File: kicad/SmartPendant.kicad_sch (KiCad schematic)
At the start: 64 parts, among them J1 Conn_01x05, P1 FPC 0.5MM 40P Pull type H2.0m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, P2 KH-FG0.5-H2.0-6PIN, Q1 SS8050_C2150, U2 AMS1117-3.3, U3 MB85RC256VPNF

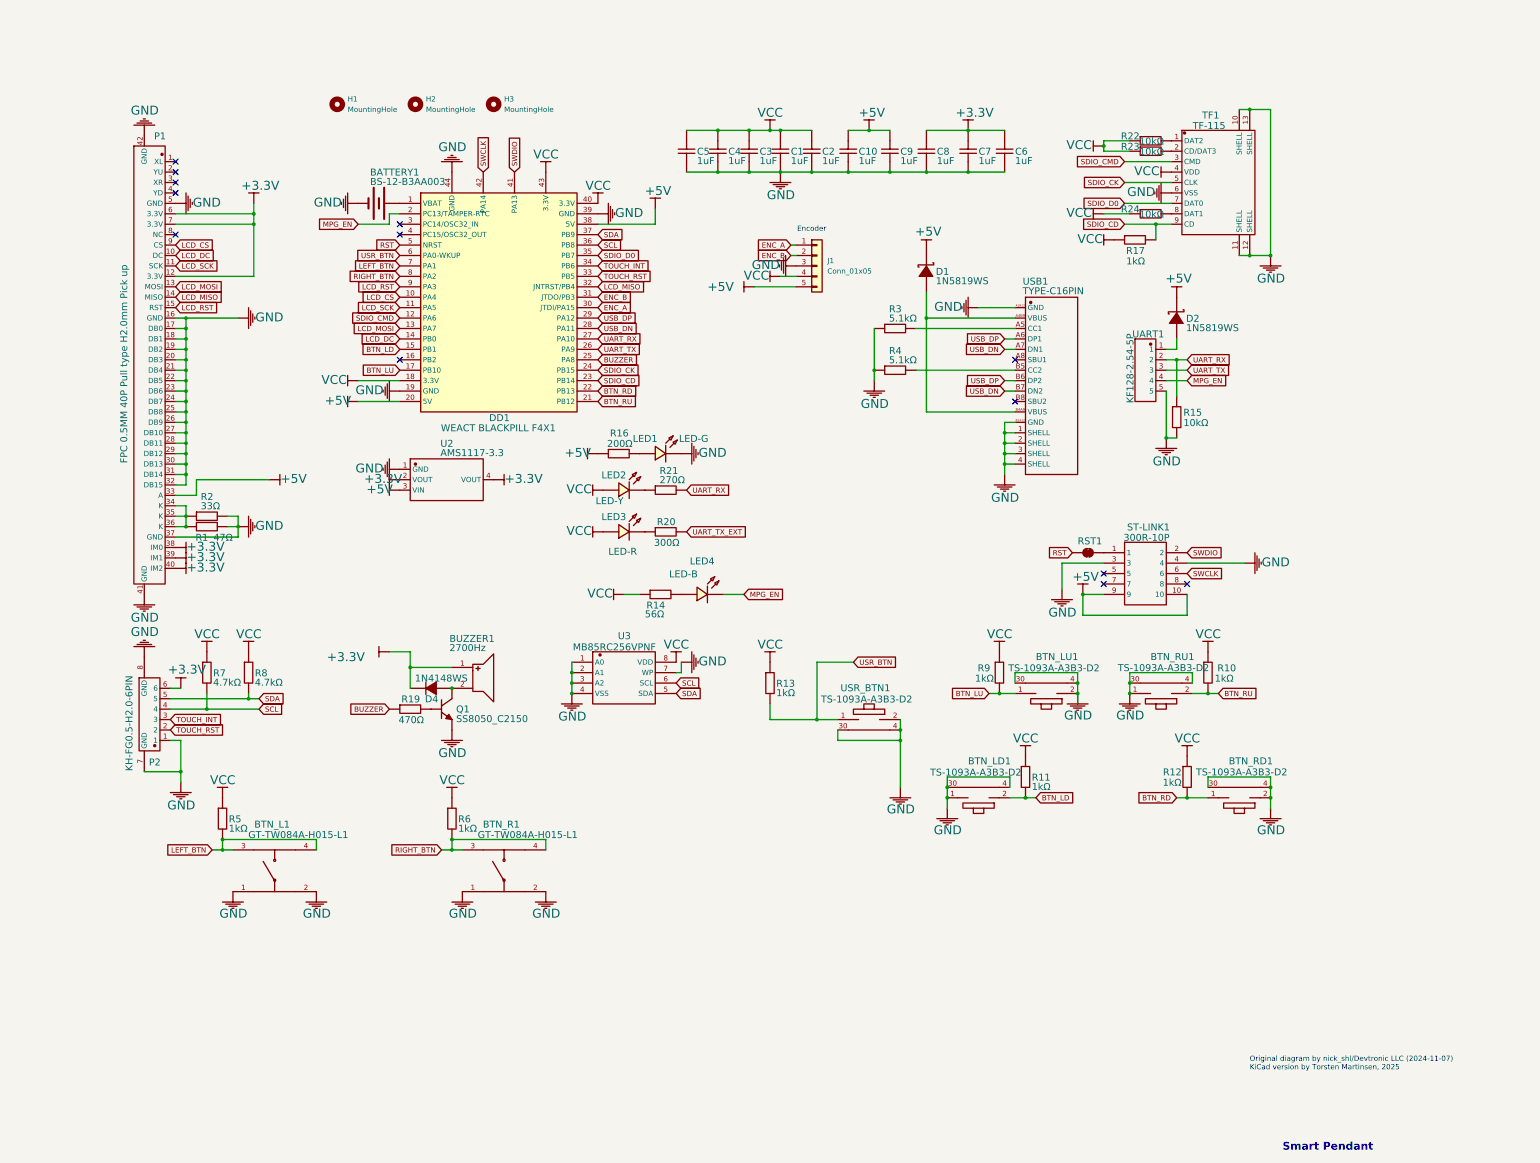
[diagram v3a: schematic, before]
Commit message: Add footprints.
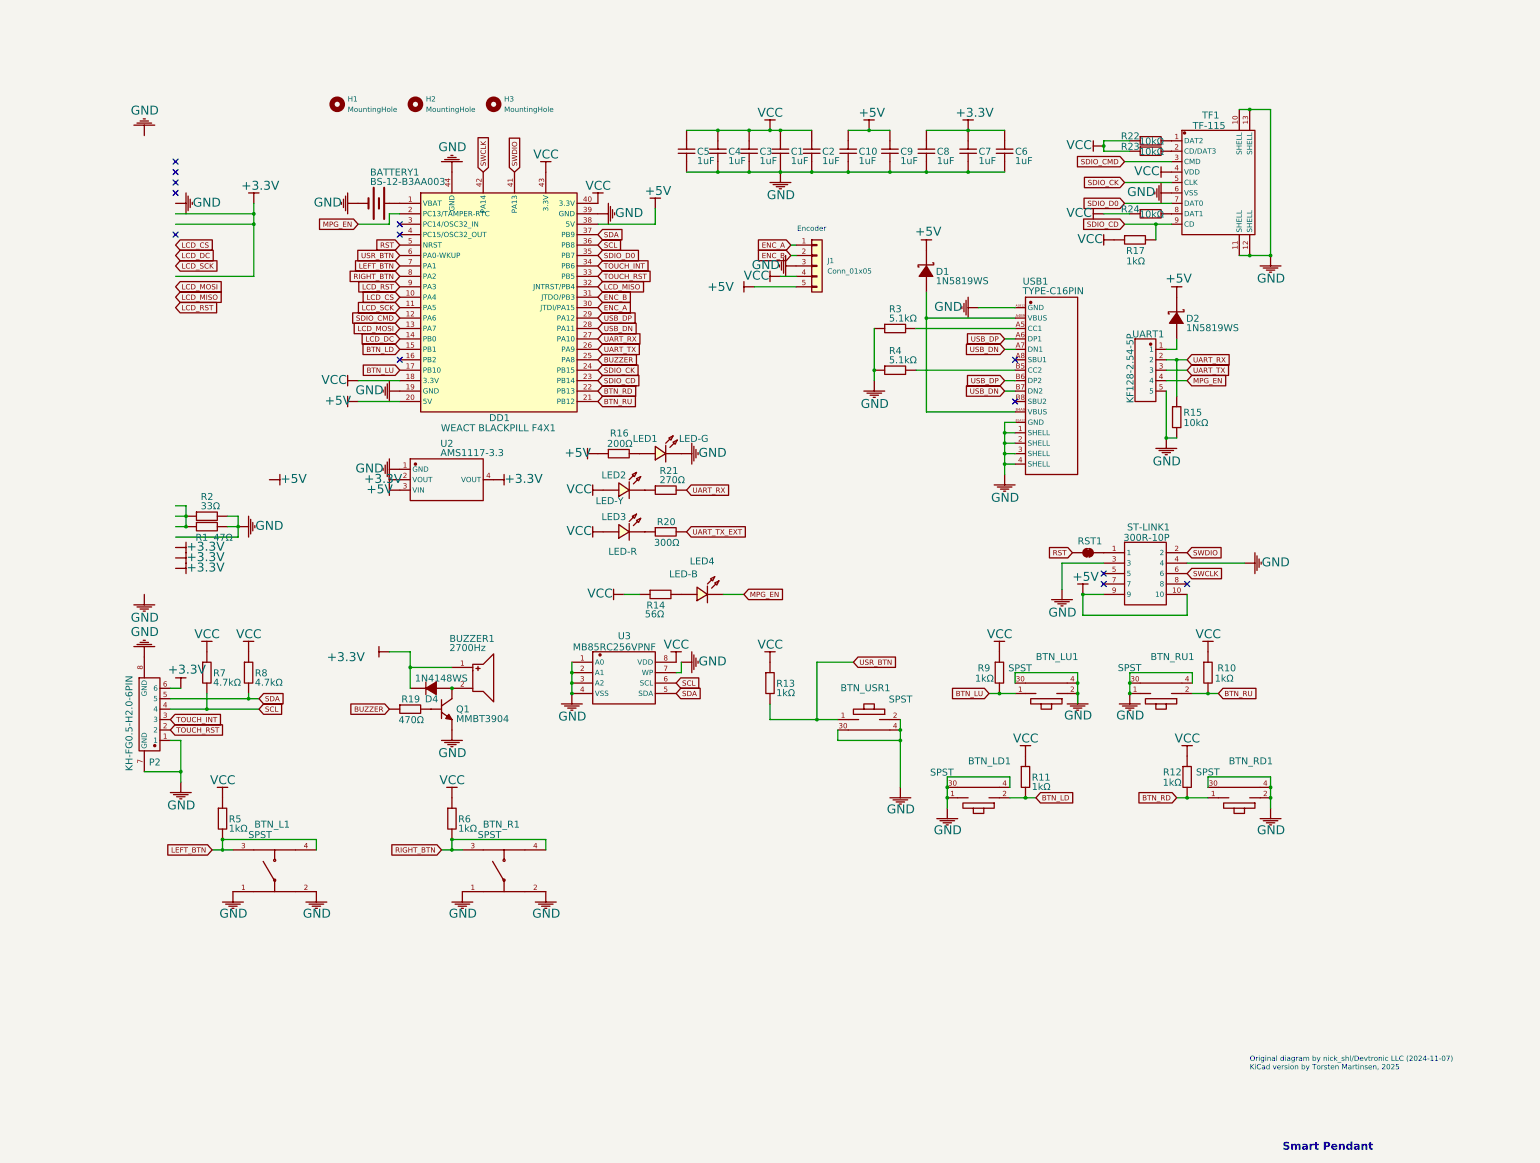
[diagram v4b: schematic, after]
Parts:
- removed P1: FPC 0.5MM 40P Pull type H2.0mm Pick up, symbol FPC 0.5MM 40P Pull type H2.0mm Pick up
- BATTERY1: footprint (none) -> Battery:BatteryHolder_Keystone_1060_1x2032
- BTN_L1, BTN_R1: value GT-TW084A-H015-L1 -> SPST
- BTN_LD1, BTN_LU1, BTN_RD1, BTN_RU1: value TS-1093A-A3B3-D2 -> SPST
- BTN_USR1: renamed from USR_BTN1; value TS-1093A-A3B3-D2 -> SPST
- Q1: value SS8050_C2150 -> MMBT3904; footprint (none) -> PCM_Package_TO_SOT_SMD_AKL:SOT-23
- TF1: footprint (none) -> Custom:J_SD_Card-micro_socket_A
- UART1: footprint (none) -> Connector_JST:JST_XH_B5B-XH-A_1x05_P2.50mm_Vertical

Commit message: Make side switch footprint.
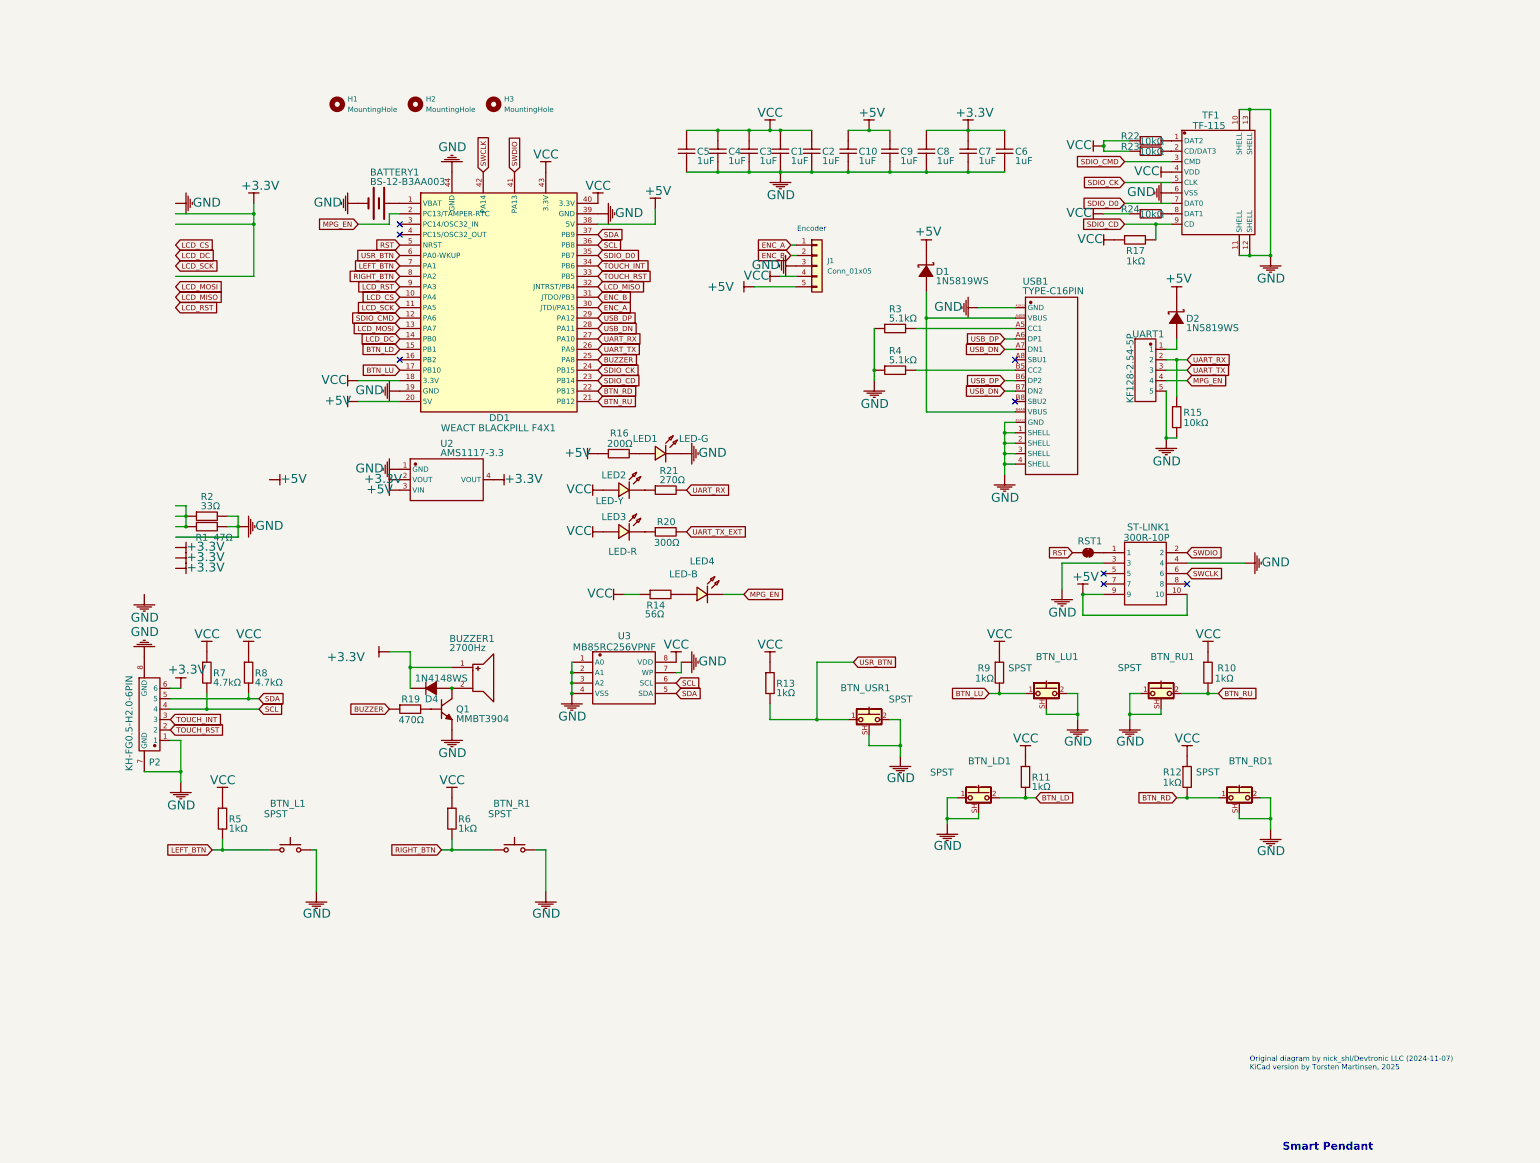
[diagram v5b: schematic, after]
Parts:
- BTN_L1: symbol GT-TW084A-H015-L1 -> Switch:SW_Push
- BTN_LD1: footprint (none) -> SmartPendant:SMD_Push_Side_button_3x6x3.5mm; symbol TS-1093A-A3B3-D2_4 -> Switch:SW_Push_Shielded
- BTN_LU1: footprint (none) -> SmartPendant:SMD_Push_Side_button_3x6x3.5mm; symbol TS-1093A-A3B3-D2_2 -> Switch:SW_Push_Shielded
- BTN_R1: symbol GT-TW084A-H015-L1_1 -> Switch:SW_Push
- BTN_RD1: footprint (none) -> SmartPendant:SMD_Push_Side_button_3x6x3.5mm; symbol TS-1093A-A3B3-D2 -> Switch:SW_Push_Shielded
- BTN_RU1: footprint (none) -> SmartPendant:SMD_Push_Side_button_3x6x3.5mm; symbol TS-1093A-A3B3-D2_3 -> Switch:SW_Push_Shielded
- BTN_USR1: footprint (none) -> SmartPendant:SMD_Push_Side_button_3x6x3.5mm; symbol TS-1093A-A3B3-D2_1 -> Switch:SW_Push_Shielded
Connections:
- net GND: now also BTN_LD1.SH (B), BTN_LU1.SH (B), BTN_RD1.SH (B), BTN_RU1.SH (B), BTN_USR1.SH (B); no longer BTN_L1.1, BTN_LD1.30 (3), BTN_LD1.4, BTN_LU1.30 (3), BTN_LU1.4, BTN_R1.1, BTN_RD1.30 (3), BTN_RD1.4, BTN_RU1.30 (3), BTN_RU1.4, BTN_USR1.30 (3), BTN_USR1.4
- net LEFT_BTN: now also BTN_L1.1; no longer BTN_L1.3, BTN_L1.4
- net RIGHT_BTN: now also BTN_R1.1; no longer BTN_R1.3, BTN_R1.4
- no-connect marks 13 -> 8

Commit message: Remove LEDs.
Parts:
- removed LED1: LED-G, PCM_Diode_SMD_AKL:D_0603_1608Metric, symbol LED-0805_G_1
- removed LED2: LED-Y, PCM_Diode_SMD_AKL:D_0603_1608Metric, symbol LED-0805_G
- removed LED3: LED-R, PCM_Diode_SMD_AKL:D_0603_1608Metric, symbol LED-0805_R
- removed LED4: LED-B, PCM_Diode_SMD_AKL:D_0603_1608Metric, symbol LED-0805_B
- removed R14: 56Ω, PCM_Resistor_SMD_AKL:R_0603_1608Metric, symbol 0805W8F1002T5E_17
- removed R16: 200Ω, PCM_Resistor_SMD_AKL:R_0603_1608Metric, symbol 0805W8F3000T5E
- removed R20: 300Ω, PCM_Resistor_SMD_AKL:R_0603_1608Metric, symbol 0805W8F1000T5E
- removed R21: 270Ω, PCM_Resistor_SMD_AKL:R_0603_1608Metric, symbol 0805W8F2700T5E
- J1: renamed from UART1; value KF128-2.54-5P -> UART
- J2: renamed from ST-LINK1; value 300R-10P -> ST-LINK; footprint (none) -> Connector_IDC:IDC-Header_2x05_P2.54mm_Horizontal
- renumbered J1 to J3, USB1 to J4

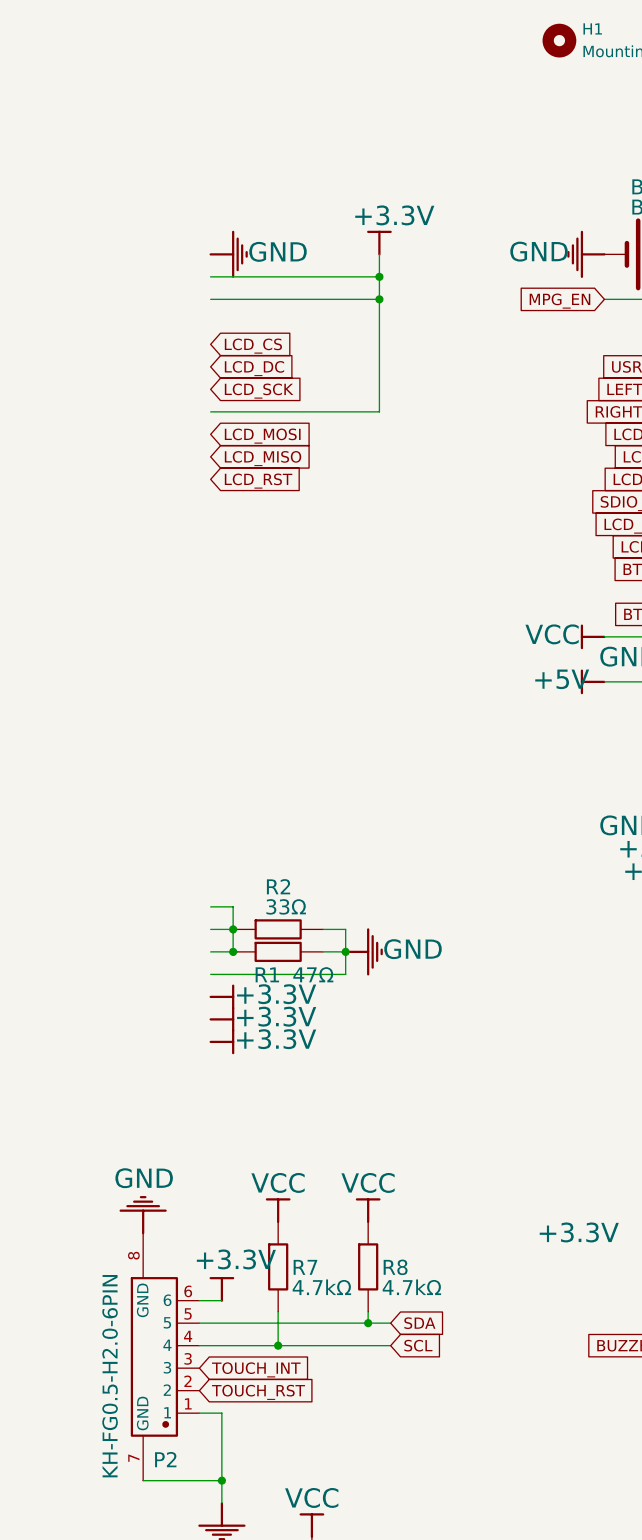
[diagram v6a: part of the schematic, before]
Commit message: Add new display connector.
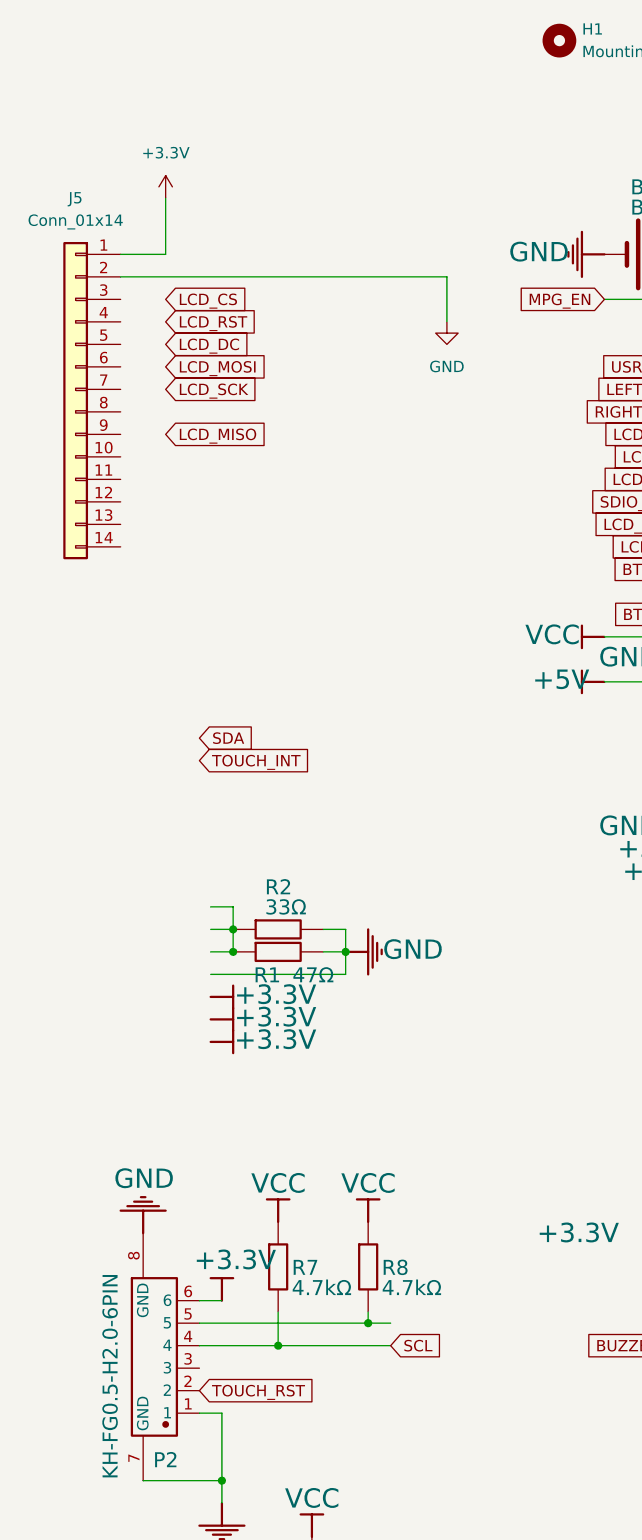
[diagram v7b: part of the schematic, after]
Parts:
- added J5: Conn_01x14, symbol Connector_Generic:Conn_01x14
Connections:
- net +3.3V: now also J5.1 (Pin_1)
- net GND: now also J5.2 (Pin_2)
- net SDA: no longer P2.5, R8.2
- net TOUCH_INT: no longer P2.3
- new net: P2.5, R8.2
